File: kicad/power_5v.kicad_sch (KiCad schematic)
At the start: 24 parts, among them U9 AP64501SP-13

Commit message: GPIO connectors defined
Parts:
- C52, C65: footprint PCM_JLCPCB:C_0402 -> MyParts:C0402; symbol PCM_JLCPCB-Capacitors:0402,100nF -> MyParts:CL05B104KO5NNNC_ALT; Attrition Qty 10 -> (none); Capacitance 100nF -> (none); Category Capacitors,Multilayer Ceramic Capacitors MLCC - SMD/SMT -> (none); Class Basic Component -> (none); LCSC C1525 -> (none); LCSC Part (none) -> C1525; MPN (none) -> CL05B104KO5NNNC; Manufacturer Samsung Electro-Mechanics -> SAMSUNG; Minimum Qty 20 -> (none); Part CL05B104KO5NNNC -> (none); Price 0.004USD -> (none); Process SMT -> (none); Stock 20208285 -> (none); Temperature Coefficient X7R -> (none); Voltage Rated 16V -> (none); Voltage Rating (none) -> 16V
- C53, C54, C55, C56: Manufacturer SAMSUNG(三星) -> SAMSUNG; Tolerance (none) -> ±10%; Voltage Rating (none) -> 10V
- C57: value 100uF 6.3V -> 100uF; symbol Device:C_Polarized -> MyParts:EEFCX0J101R; Tolerance (none) -> ±20%; Voltage Rating (none) -> 6.3V
- C59, C60, C61, C62, C63, C64: Manufacturer muRata(村田) -> muRata; Tolerance (none) -> ±10%; Voltage Rating (none) -> 35V
- C67: Manufacturer YAGEO(国巨) -> YAGEO; Tolerance (none) -> ±10%; Voltage Rating (none) -> 50V
- L4: value SRN6045TA-3R3Y -> 3.3uH; Current Rating (none) -> 5A; DC Resistance (none) -> 21mΩ; Saturation Current (none) -> 7.8A; Tolerance (none) -> ±30%
- R75: Manufacturer UNI-ROYAL(厚声) -> UNI-ROYAL; Tolerance (none) -> ±1%; Voltage Rating (none) -> 200V
- R76: Manufacturer FOJAN(富捷) -> FOJAN; Voltage Rating (none) -> 50V
- R77: symbol PCM_JLCPCB-Resistors:0402,20kΩ -> MyParts:0402WGF2002TCE; Attrition Qty 10 -> (none); Category Resistors,Chip Resistor - Surface Mount -> (none); Class Basic Component -> (none); LCSC C25765 -> (none); LCSC Part (none) -> C25765; MPN (none) -> 0402WGF2002TCE; Manufacturer UNI-ROYAL(Uniroyal Elec) -> UNI-ROYAL; Minimum Qty 20 -> (none); Operating Temperature Range -55°C~+155°C -> (none); Overload Voltage (Max) 50V -> (none); Part 0402WGF2002TCE -> (none); Power(Watts) 62.5mW -> (none); Price 0.004USD -> (none); Process SMT -> (none); Resistance 20kΩ -> (none); Stock 3268540 -> (none); Temperature Coefficient ±100ppm/°C -> (none); Type Thick Film Resistors -> (none); Voltage Rating (none) -> 50V
- R78: symbol PCM_JLCPCB-Resistors:0402,2.2kΩ -> MyParts:0402WGF2201TCE; Attrition Qty 10 -> (none); Category Resistors,Chip Resistor - Surface Mount -> (none); Class Basic Component -> (none); LCSC C25879 -> (none); LCSC Part (none) -> C25879; MPN (none) -> 0402WGF2201TCE; Manufacturer UNI-ROYAL(Uniroyal Elec) -> UNI-ROYAL; Minimum Qty 20 -> (none); Operating Temperature Range -55°C~+155°C -> (none); Overload Voltage (Max) 50V -> (none); Part 0402WGF2201TCE -> (none); Power(Watts) 62.5mW -> (none); Price 0.004USD -> (none); Process SMT -> (none); Resistance 2.2kΩ -> (none); Stock 1767502 -> (none); Temperature Coefficient ±100ppm/°C -> (none); Type Thick Film Resistors -> (none); Voltage Rating (none) -> 50V
- TP8: Manufacturer 荣和 -> ronghe
- U9: Manufacturer DIODES(美台) -> DIODES

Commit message: schematic cleanup
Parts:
- added TP19, TP24: TestPoint_Small, TestPoint:TestPoint_Pad_D1.5mm, symbol Connector:TestPoint_Small
- C18: value 0.1uF -> 100nF; footprint PCM_SparkFun-Capacitor:C_0603_1608Metric -> MyParts:C0603; symbol PCM_SparkFun-Capacitor:0.1uF_0603_25V_20% -> MyParts:CC0603KRX7R9BB104; LCSC Part (none) -> C14663; MPN (none) -> CC0603KRX7R9BB104; Manufacturer (none) -> YAGEO; PROD_ID CAP-00810 -> (none); Tolerance 20% -> ±10%; Voltage 25V -> (none); Voltage Rating (none) -> 50V
- C53, C54, C55, C56: value 10uF 10V -> 10uF
- C59, C60, C61, C62, C63, C64: value 10uF 35V -> 10uF
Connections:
- net GND: now also TP24.1
- net at C58.2, R76.1, R78.1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: now also TP19.1

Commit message: Still refining
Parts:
- C18: Pkg Type (none) -> SMD 0603
- C52, C58, C65, C66, C67, R76, R77, R78: Pkg Type (none) -> SMD 0402
- C53, C54, C55, C56, C59, C60, C61, C62, C63, C64: Pkg Type (none) -> SMD 0805
- C57: Pkg Type (none) -> SMD EIA-7343 (D case)
- L4: Pkg Type (none) -> SMD Power inductor 6.0x6.0
- R75: Pkg Type (none) -> SMD 1206
- TP19, TP24: Pkg Type (none) -> SMD Test pad D1.5
- TP8: Pkg Type (none) -> SMD Test point loop
- U9: Pkg Type (none) -> SMD SOIC-8 EP

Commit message: Mods
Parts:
- added TP33: TestPoint_Small, TestPoint:TestPoint_Pad_D1.5mm, symbol Connector:TestPoint_Small
- L4: footprint MyParts:IND-SMD_L6.0-W6.0 -> MyParts:IND-SMD_L7.3-W6.6_SRP7028A; symbol MyParts:SRN6045TA-3R3Y -> MyParts:SRP7028A-3R3M; Current Rating 5A -> 6A; DC Resistance 21mΩ -> 30mΩ; LCSC Part C3221229 -> C913186; MPN SRN6045TA-3R3Y -> SRP7028A-3R3M; Pkg Type SMD Power inductor 6.0x6.0 -> SMD Power inductor 7.3x6.6; Saturation Current 7.8A -> 12A; Tolerance ±30% -> ±20%
- R76: value 11.5kΩ -> 12kΩ; symbol MyParts:FRC0402F1152TS -> MyParts:RT0402BRD0712KL; LCSC Part C2933068 -> C784579; MPN FRC0402F1152TS -> RT0402BRD0712KL; Manufacturer FOJAN -> YAGEO; Tolerance ±1% -> ±0.1%
- R78: symbol MyParts:0402WGF2201TCE -> MyParts:RT0402BRD072K2L; LCSC Part C25879 -> C326602; MPN 0402WGF2201TCE -> RT0402BRD072K2L; Manufacturer UNI-ROYAL -> YAGEO; Tolerance ±1% -> ±0.1%
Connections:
- net GND: now also TP33.1
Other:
- note added: "+5v @ 3A PSU ( 8.3v-19v Input )"
- note added: "12V to 5V Buck - AP64501 (5A, 570kHz, 0.8V reference) Vout = 5.16V, designed for 3A. Input 8.3V-19V (eFuse UVLO cuts in at 8.3V, OVP cuts out at 17.5-19V). EN tied to VIN: starts automatically, the eFuse upstream provides the UVLO. Output voltage set by the FB divider Vout = 0.8V x (1 + R76/R78) = 0.8 x (1 + 12k/2.2k) = 5.16V Corners 5.10-5.22V (Vref 792-808mV, R76/R78 0.1%). Worst-case USB VBUS 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"
- note removed: "+5v @ 3A PSU ( 8.3v-28v Input )"
- note removed: "12V to 5V Buck - AP64501 (5A, 570kHz, 0.8V reference) Vout = 4.98V, designed for 3A. Input 8.3V-28V (eFuse UVLO cuts in at 8.3V). EN tied to VIN: starts automatically, the eFuse upstream provides the UVLO. Output voltage set by the FB divider Vout = 0.8V x (1 + R76/R78) = 0.8 x (1 + 11.5k/2.2k) = 4.98V R76 11.5k 1% top leg, 5V to FB R78 2.2k 1% bottom leg, FB to GND C58 DNP optional feedforward a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"

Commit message: Ready to start layout
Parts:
- renumbered C52 to C40, C53 to C41, C54 to C42, C55 to C43, C56 to C44, C57 to C45, C58 to C46, C18 to C47, C59 to C48, C60 to C49, C61 to C50, C62 to C51, C63 to C52, C64 to C53, C65 to C54, C66 to C55, C67 to C56, L4 to L2, R75 to R41, R76 to R42, R77 to R43, R78 to R44, TP8 to TP24, TP19 to TP25, TP33 to TP26, TP24 to TP27, U9 to U15
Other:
- note added: "12V to 5V Buck - AP64501 (5A, 570kHz, 0.8V reference) Vout = 5.16V, designed for 3A. Input 8.3V-19V (eFuse UVLO cuts in at 8.3V, OVP cuts out at 17.5-19V). EN tied to VIN: starts automatically, the eFuse upstream provides the UVLO. Output voltage set by the FB divider Vout = 0.8V x (1 + R42/R44) = 0.8 x (1 + 12k/2.2k) = 5.16V Corners 5.10-5.22V (Vref 792-808mV, R42/R44 0.1%). Worst-case USB VBUS 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"
- note removed: "12V to 5V Buck - AP64501 (5A, 570kHz, 0.8V reference) Vout = 5.16V, designed for 3A. Input 8.3V-19V (eFuse UVLO cuts in at 8.3V, OVP cuts out at 17.5-19V). EN tied to VIN: starts automatically, the eFuse upstream provides the UVLO. Output voltage set by the FB divider Vout = 0.8V x (1 + R76/R78) = 0.8 x (1 + 12k/2.2k) = 5.16V Corners 5.10-5.22V (Vref 792-808mV, R76/R78 0.1%). Worst-case USB VBUS 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"

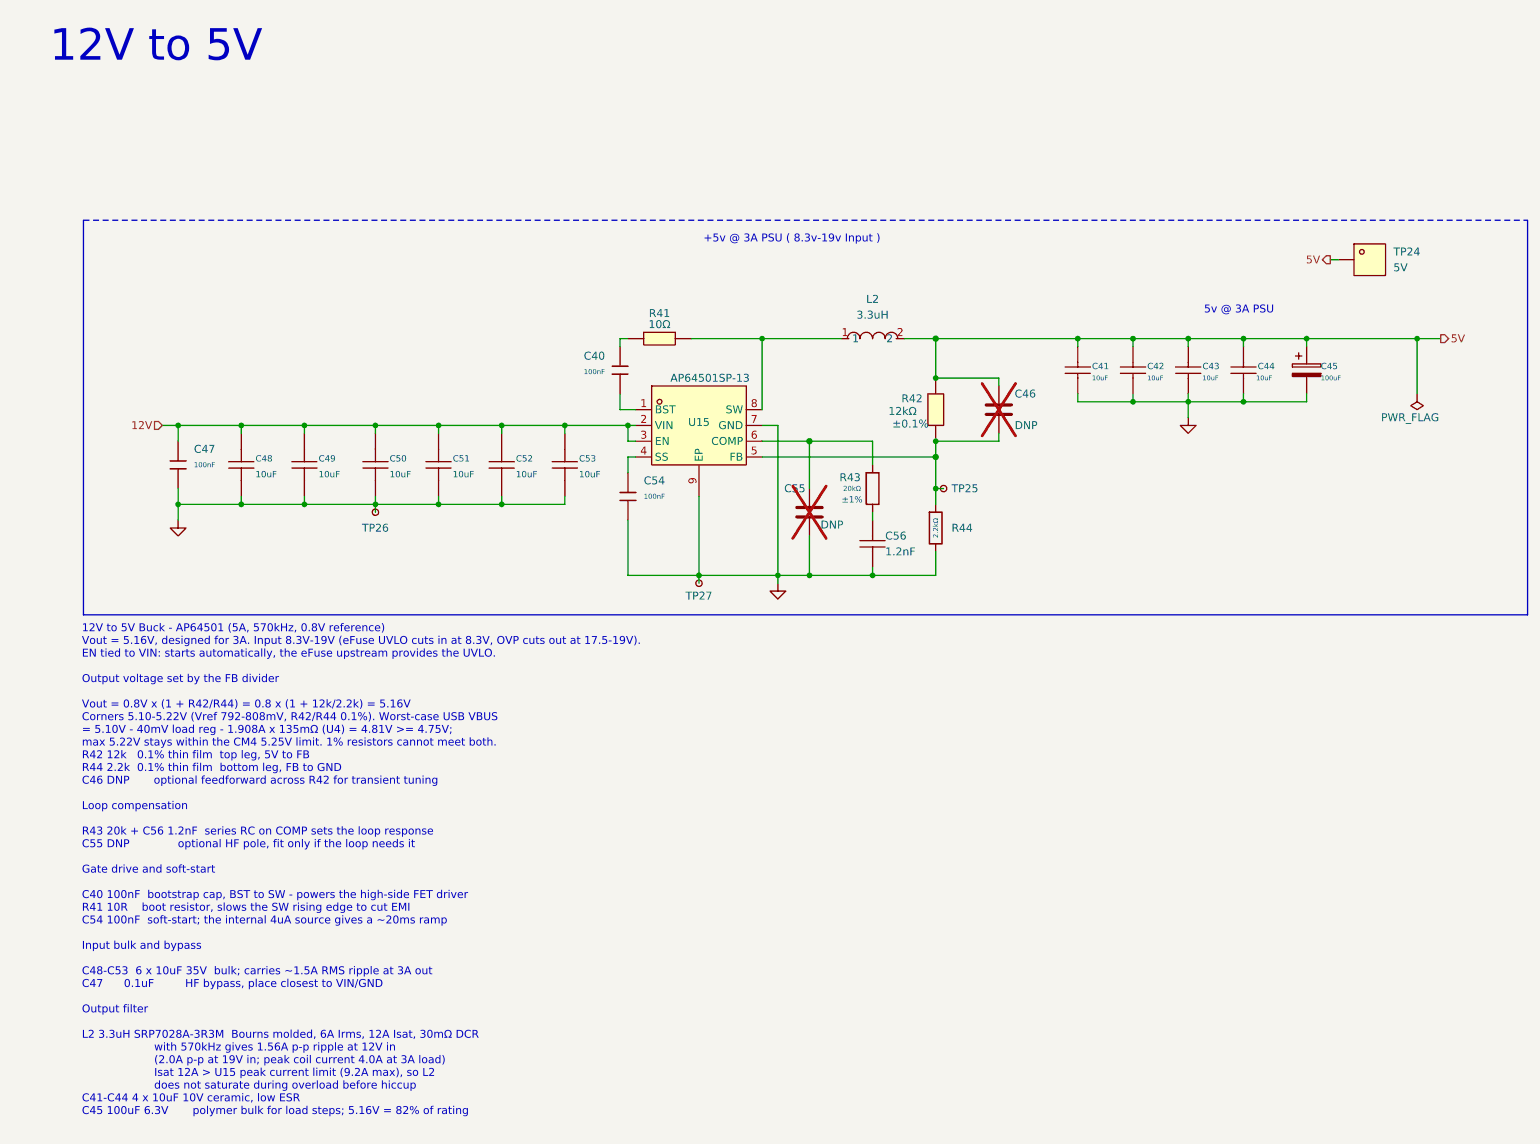
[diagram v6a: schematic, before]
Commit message: IPC footprint renaming, battery sim added
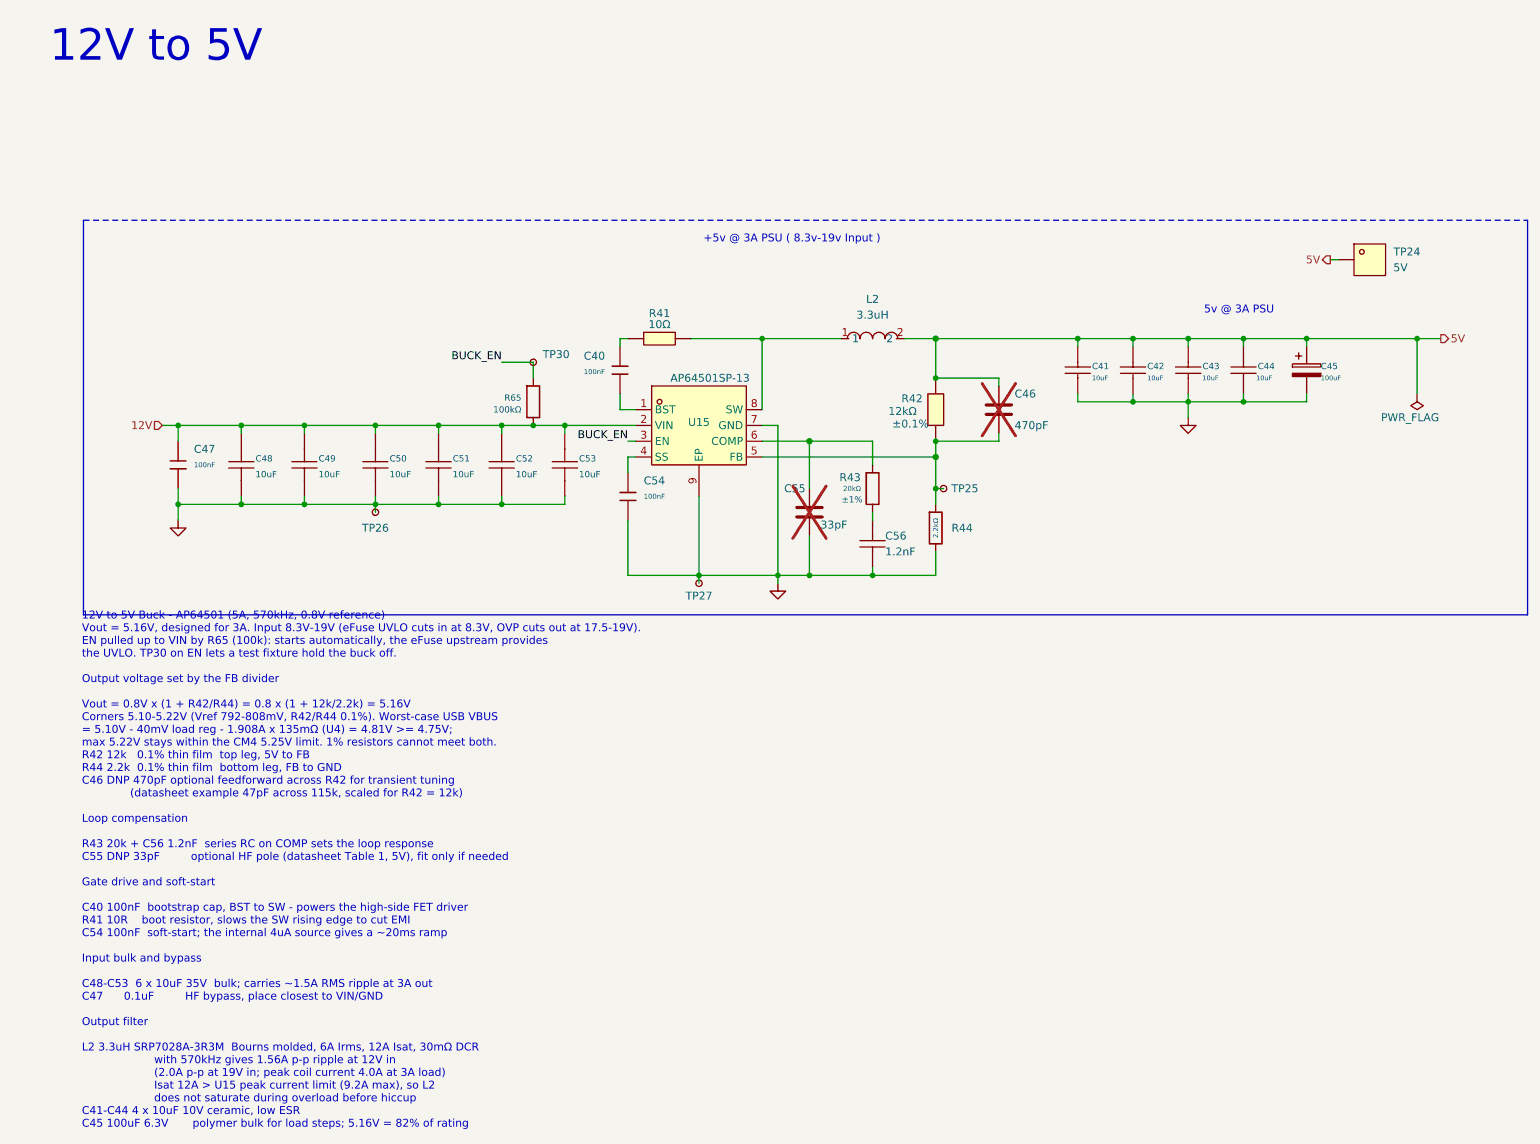
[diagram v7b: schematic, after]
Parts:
- added R65: 100kΩ, MyPartsIPC:RESC1005X40N, symbol MyParts:0402WGF1003TCE
- added TP30: TestPoint_Small, TestPoint:TestPoint_Pad_D1.5mm, symbol Connector:TestPoint_Small
- C40, C54, C56: footprint MyParts:C0402 -> MyPartsIPC:CAPC1005X55N
- C41, C42, C43, C44, C48, C49, C50, C51, C52, C53: footprint MyParts:C0805 -> MyPartsIPC:CAPC2012X145N
- C45: footprint Capacitor_Tantalum_SMD:CP_EIA-7343-31_Kemet-D -> MyPartsIPC:CAPMP7343X310N
- C46: value DNP -> 470pF; footprint MyParts:C0402 -> MyPartsIPC:CAPC1005X55N
- C47: footprint MyParts:C0603 -> MyPartsIPC:CAPC1608X95N
- C55: value DNP -> 33pF; footprint MyParts:C0402 -> MyPartsIPC:CAPC1005X55N
- L2: footprint MyParts:IND-SMD_L7.3-W6.6_SRP7028A -> MyPartsIPC:INDM7366X280N
- R41: footprint MyParts:R1206 -> MyPartsIPC:RESC3216X70N
- R42, R43, R44: footprint MyParts:R0402 -> MyPartsIPC:RESC1005X40N
- TP26: now left out of the parts list
- U15: footprint MyParts:SOIC-8_L4.9-W3.9-P1.27-LS6.0-BL-EP-1 -> MyPartsIPC:SOIC127P600X170-9N
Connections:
- net 12V: now also R65.2; no longer U15.3 (EN)
- new net BUCK_EN: R65.1, TP30.1, U15.3 (EN)
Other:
- note added: "12V to 5V Buck - AP64501 (5A, 570kHz, 0.8V reference) Vout = 5.16V, designed for 3A. Input 8.3V-19V (eFuse UVLO cuts in at 8.3V, OVP cuts out at 17.5-19V). EN pulled up to VIN by R65 (100k): starts automatically, the eFuse upstream provides the UVLO. TP30 on EN lets a test fixture hold the buck off. Output voltage set by the FB divider Vout = 0.8V x (1 + R42/R44) = 0.8 x (1 + 12k/2.2k) = 5.16V Co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"
- note removed: "12V to 5V Buck - AP64501 (5A, 570kHz, 0.8V reference) Vout = 5.16V, designed for 3A. Input 8.3V-19V (eFuse UVLO cuts in at 8.3V, OVP cuts out at 17.5-19V). EN tied to VIN: starts automatically, the eFuse upstream provides the UVLO. Output voltage set by the FB divider Vout = 0.8V x (1 + R42/R44) = 0.8 x (1 + 12k/2.2k) = 5.16V Corners 5.10-5.22V (Vref 792-808mV, R42/R44 0.1%). Worst-case USB VBUS 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"

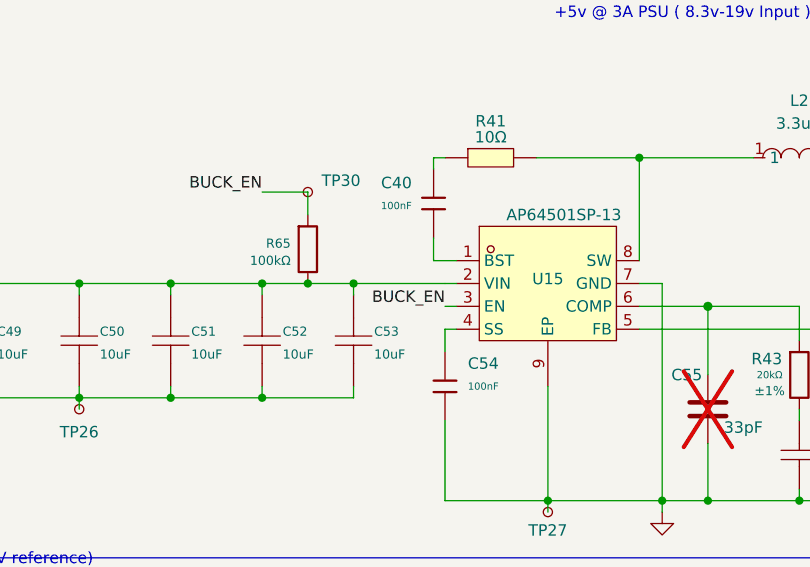
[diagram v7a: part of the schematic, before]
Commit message: Updates after latest Tomachie review
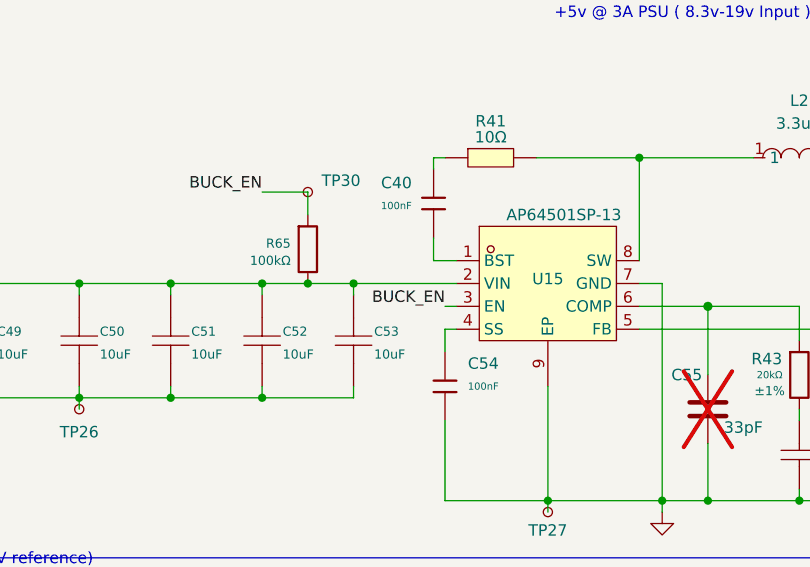
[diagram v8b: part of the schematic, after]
